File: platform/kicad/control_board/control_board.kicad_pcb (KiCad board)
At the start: 2 copper layers, 51 parts, among them J1 DHT22, J10 USB_PWR_IN, J11 UART, J12 ADC1,6, J13 24V/5V OUT, J14 PoE 1, J15 PoE 2, J16 PoE 3, J17 Barrel_Jack, J18 ADC1,7, J19 ROUTER 24V, J2 DS18B20, J3 Qwiic JST, J4 Qwiic JST, J5 Nav Light, J6 24V IN, J7 RJ45 IN - 1, J8 RJ45 IN - 2, J9 RJ45 IN - 3, K0 LCA717, K1 LCA717, K2 LCA717, K3 LCA717, M1 STEPDOWN->5V, U2 ESP32-DevKitC, U3 ACS722xLCTR-20AU

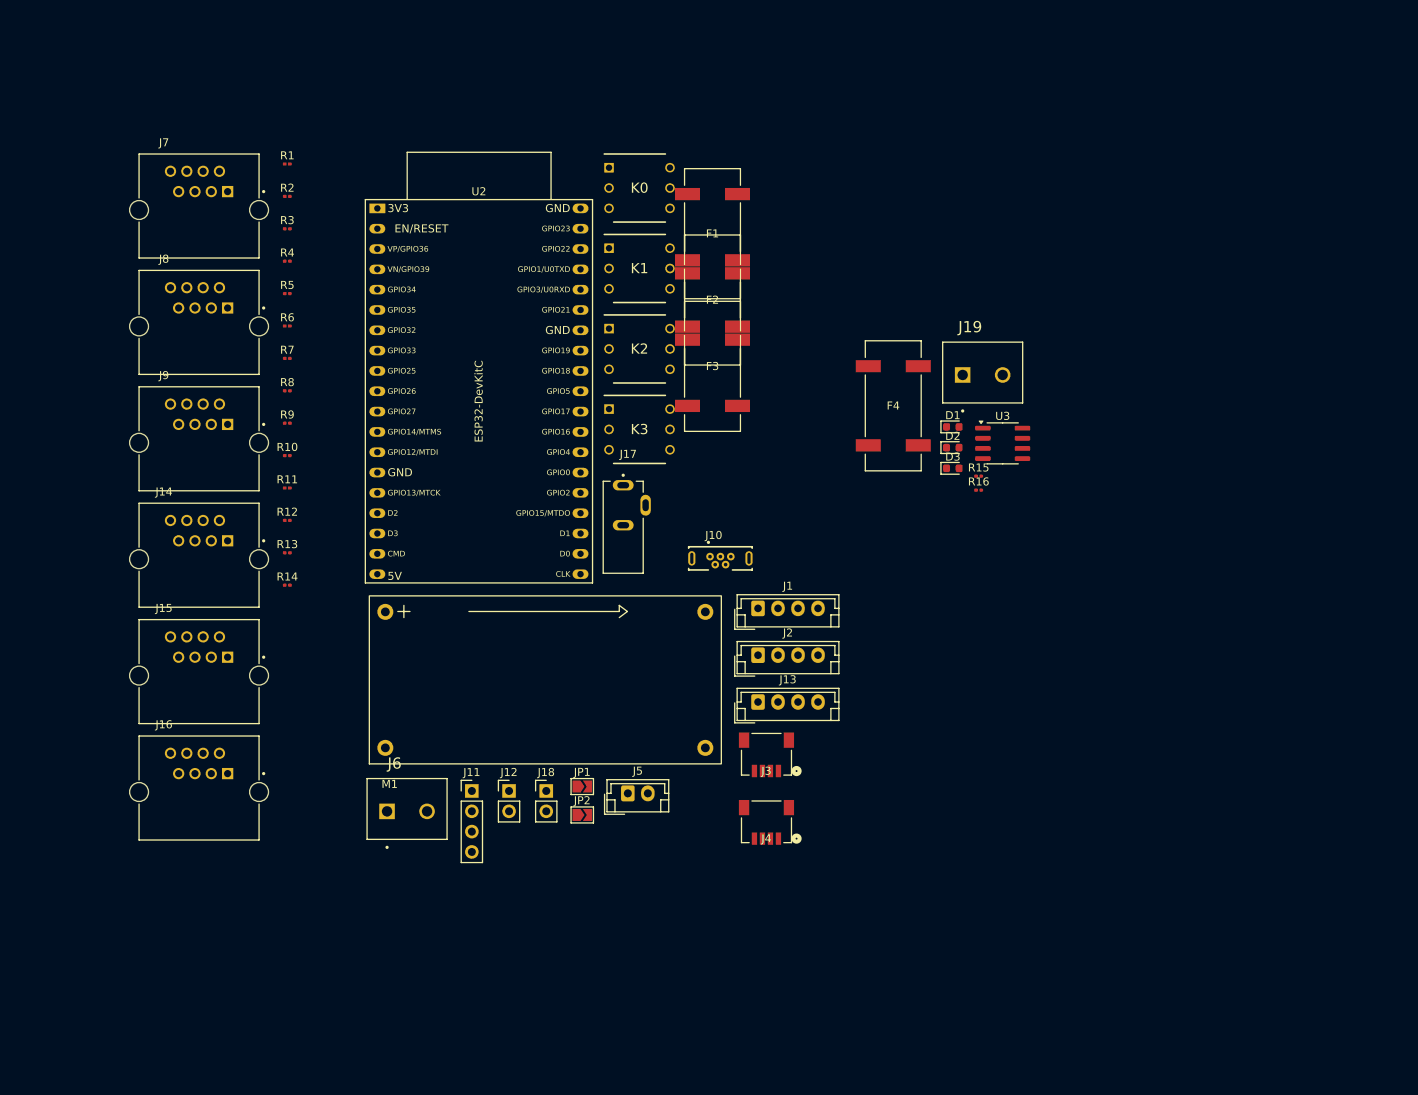
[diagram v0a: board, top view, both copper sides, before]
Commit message: Control Board: Add all 3d models and complete initial layout (#3)
This change adds a new models directory which contains the 3d models for the footprints used in PCBs.
This change also completes a draft layout for the new PCB.
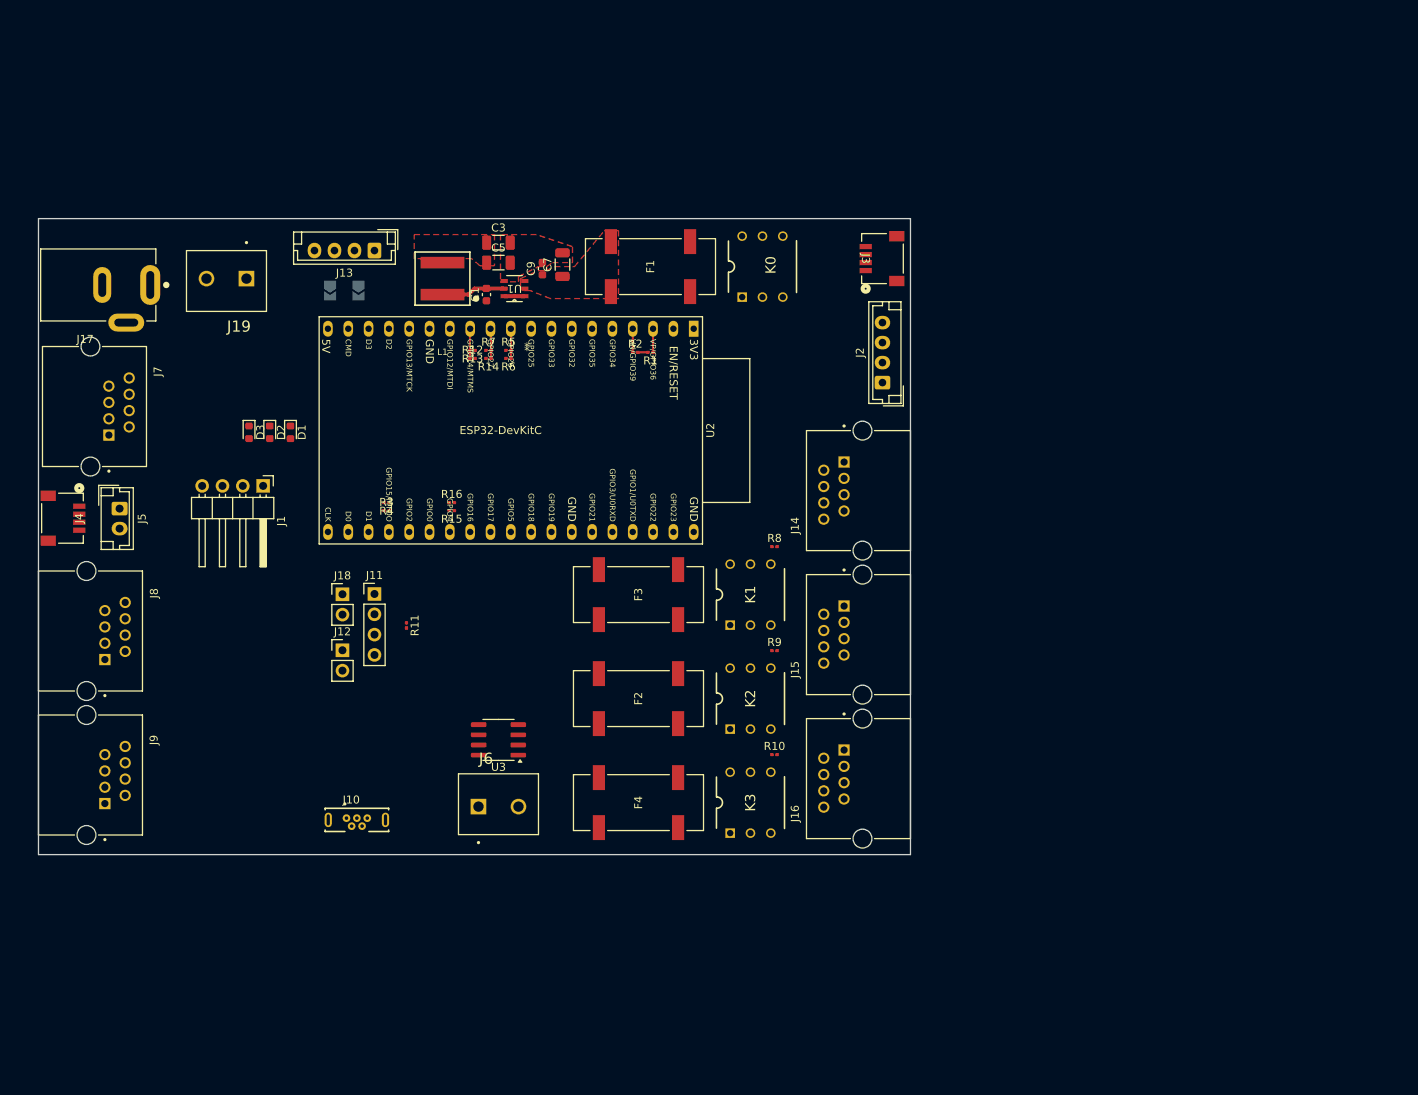
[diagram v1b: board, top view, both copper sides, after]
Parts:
- removed M1: STEPDOWN->5V, AusOcean:LM2596_Step_Down_Module
- added C1: 0.1u, Capacitor_SMD:C_0603_1608Metric, F.Cu at (143.0, 59.5)
- added C3: 22u, Capacitor_SMD:C_1206_3216Metric, F.Cu at (144.5, 53.0)
- added C5: 22u, Capacitor_SMD:C_1206_3216Metric, F.Cu at (144.5, 55.5)
- added C7: 10u, Capacitor_SMD:C_1206_3216Metric, F.Cu at (152.5, 55.8)
- added C9: 0.1u, Capacitor_SMD:C_0603_1608Metric, F.Cu at (150.0, 56.2)
- added L1: 6.8u, AusOcean:WE-XHMI_6060, F.Cu at (137.5, 57.5)
- added U1: AP63205WU-7, AusOcean:SOIC_05WU-7_DIO, F.Cu at (146.5, 58.8)
- J1: footprint Connector_JST:JST_EH_B4B-EH-A_1x04_P2.50mm_Vertical -> Connector_PinHeader_2.54mm:PinHeader_1x04_P2.54mm_Horizontal
- J17: value Barrel_Jack -> PJ-002A; footprint AusOcean:3.5x1.35mm_Barrel_Jack_Port -> AusOcean:CUI_PJ-002A
- JP1, JP2: moved to B.Cu
- moved J4 95.8 mm to (90.0, 87.5), turned to 90 degrees
- moved J19 90.3 mm to (113.0, 57.5), turned to 180 degrees
- moved D3 88.1 mm to (113.3, 76.7), turned to -90 degrees
- moved D2 85.4 mm to (115.9, 76.7), turned to -90 degrees
- moved J14 83.4 mm to (190.0, 84.0), turned to 90 degrees
- moved J15 83.1 mm to (190.0, 102.0), turned to 90 degrees
- moved J16 82.9 mm to (190.0, 120.0), turned to 90 degrees
- moved D1 82.8 mm to (118.5, 76.7), turned to -90 degrees
- moved J13 74.0 mm to (129.0, 54.0), turned to 180 degrees
- moved U3 73.1 mm to (144.5, 115.2), turned to 180 degrees
- moved J5 72.8 mm to (97.1, 86.2), turned to -90 degrees
- moved R10 71.5 mm to (179.0, 117.0)
- moved JP2 71.3 mm to (127.0, 59.0), turned to -90 degrees
- moved JP1 69.6 mm to (123.5, 59.0), turned to -90 degrees
- moved R9 67.2 mm to (179.0, 104.0)
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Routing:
- net Net-(U1-SW): track 0.00 -> 8.01 mm
- net _P2_out: track 0.00 -> 3.73 mm
- net _P3_out: track 0.00 -> 3.71 mm
- net _P1_out: track 0.00 -> 3.71 mm
- net SST: track 0.00 -> 2.95 mm
- net DHT: track 0.00 -> 2.95 mm
- net Net-(U1-BST): track 0.00 -> 2.60 mm
- net 5VIN: track 0.00 -> 1.26 mm
- added copper zone on F.Cu, net GND
- added copper zone on F.Cu, net NW_5V
- added copper zone on F.Cu, net NW_out
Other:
- board outline added: 109 x 79.5 mm

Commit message: Control PCB: Update layout (#3)
This change updates the layout of the PCB to revise the feedback from the previous iteration.
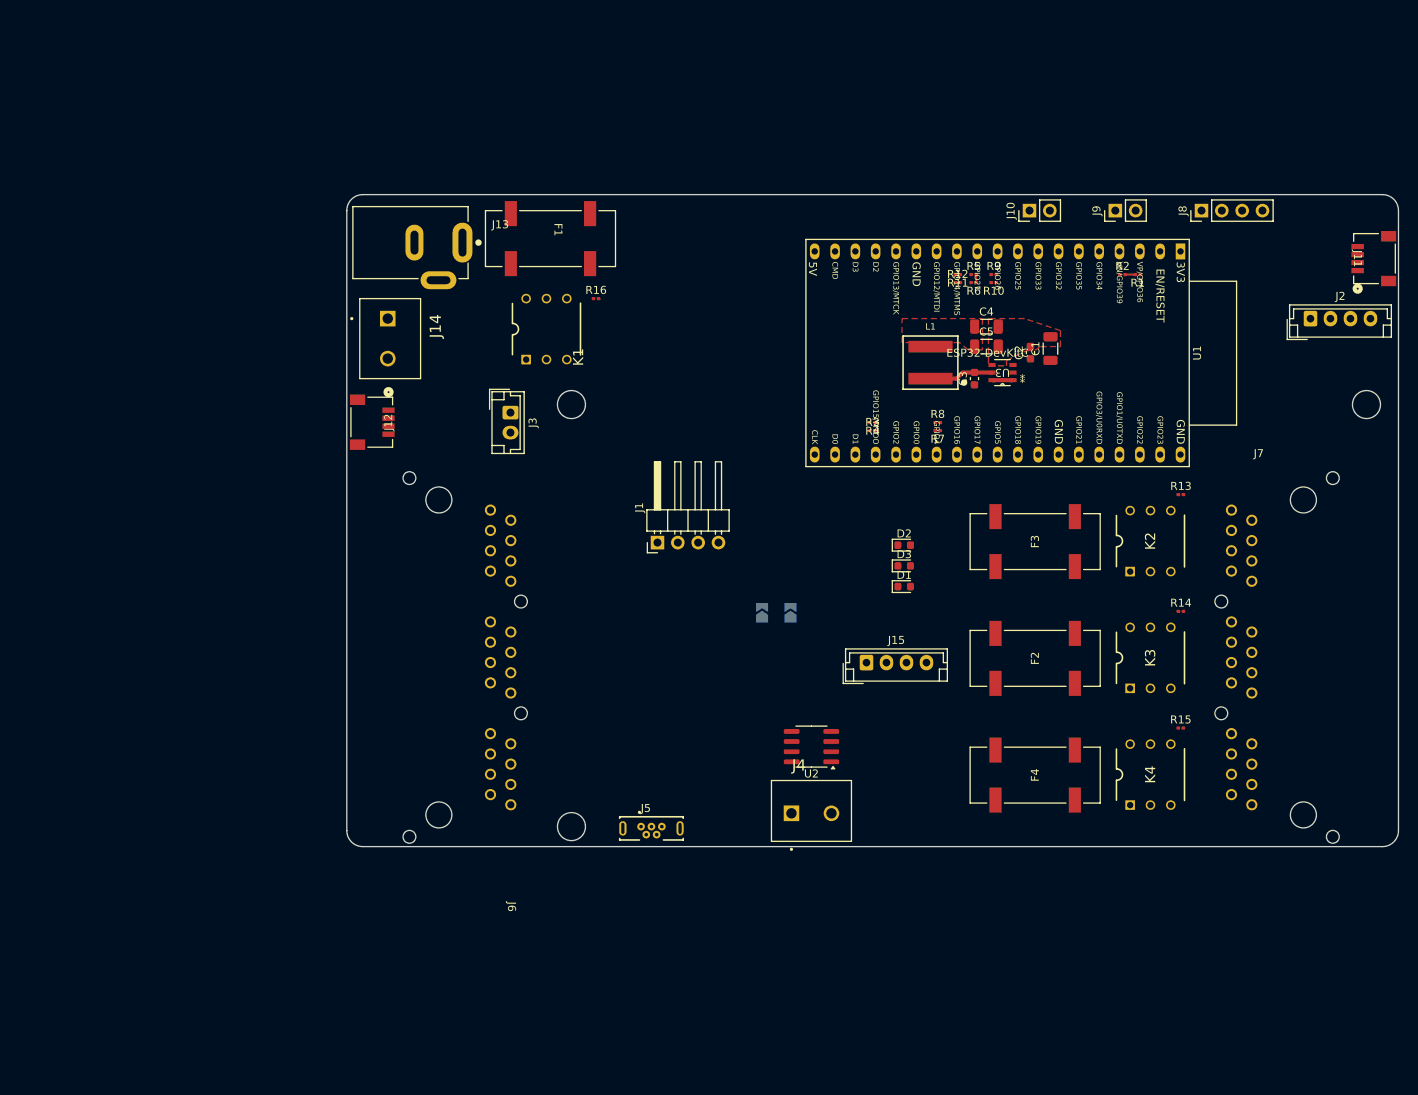
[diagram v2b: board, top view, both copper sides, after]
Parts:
- removed the J14 at (190.0, 84.0)
- removed the J15 at (190.0, 102.0)
- removed J16: PoE 3, AusOcean:RJ45_Socket
- removed the J8 at (93.0, 101.5)
- removed the J9 at (93.0, 119.5)
- added J6: ~, AusOcean:RJ45 3-port jack, F.Cu at (126.2, 82.3)
- J7: value RJ45 IN - 1 -> ~; footprint AusOcean:RJ45_Socket -> AusOcean:RJ45 3-port jack
- moved J7 171.2 mm to (256.0, 127.4), turned to 90 degrees
- moved J8 113.9 mm to (232.4, 49.0), turned to 90 degrees
- moved J9 111.1 mm to (221.6, 49.0), turned to 90 degrees
- moved J10 98.4 mm to (210.9, 49.0), turned to 90 degrees
- moved D1 84.1 mm to (195.2, 96.0), turned to 0 degrees
- moved D3 81.0 mm to (195.2, 93.4), turned to 0 degrees
- moved J15 80.2 mm to (190.5, 105.5), turned to 0 degrees
- moved D2 78.0 mm to (195.2, 90.8), turned to 0 degrees
- moved JP1 70.2 mm to (181.0, 99.3), turned to 90 degrees
- moved JP2 64.6 mm to (177.4, 99.3), turned to 90 degrees
- moved C1 61.9 mm to (213.5, 66.2)
- moved C2 61.9 mm to (211.0, 66.8)
- moved C3 61.9 mm to (204.0, 70.0)
- moved C4 61.9 mm to (205.5, 63.5)
- moved C5 61.9 mm to (205.5, 66.0)
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- renumbered C7 to C1, C9 to C2, C1 to C3, C3 to C4, D3 to D1, D1 to D2, D2 to D3, J18 to J10, J3 to J11, J4 to J12, J17 to J13, J19 to J14, J13 to J15, J5 to J3, J6 to J4, J10 to J5, J11 to J8, J12 to J9, K0 to K1, K1 to K2, K2 to K3, K3 to K4, R6 to R10, R13 to R11, R8 to R13, R9 to R14, R10 to R15, R11 to R16, R7 to R5, R14 to R6, R15 to R7, R16 to R8, R5 to R9, U2 to U1, U3 to U2, U1 to U3
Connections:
- J7 pad 1: D1_Rx+ -> D3_Rx+
- J7 pad 2: D1_Rx- -> D3_Rx-
- J7 pad 3: D1_Tx+ -> D3_Tx+
- J7 pad 4: unconnected-(J7-Pad4) -> P3_out
- J7 pad 5: unconnected-(J7-Pad5) -> P3_out
- J7 pad 6: D1_Tx- -> D3_Tx-
- J7 pad 7: unconnected-(J7-Pad7) -> GND
- J7 pad 8: unconnected-(J7-Pad8) -> GND
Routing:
- net _P1_out: track 3.71 -> 0.04 mm
- net _P3_out: track 3.71 -> 0.05 mm
- net SST: track 2.95 -> 0.00 mm
- net DHT: track 2.95 -> 0.00 mm
- net _P2_out: track 3.73 -> 1.09 mm
- removed copper zone on F.Cu, net NW_out
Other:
- board size 109 x 79.5 mm -> 131.5 x 81.5 mm

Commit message: Update Control Board layout
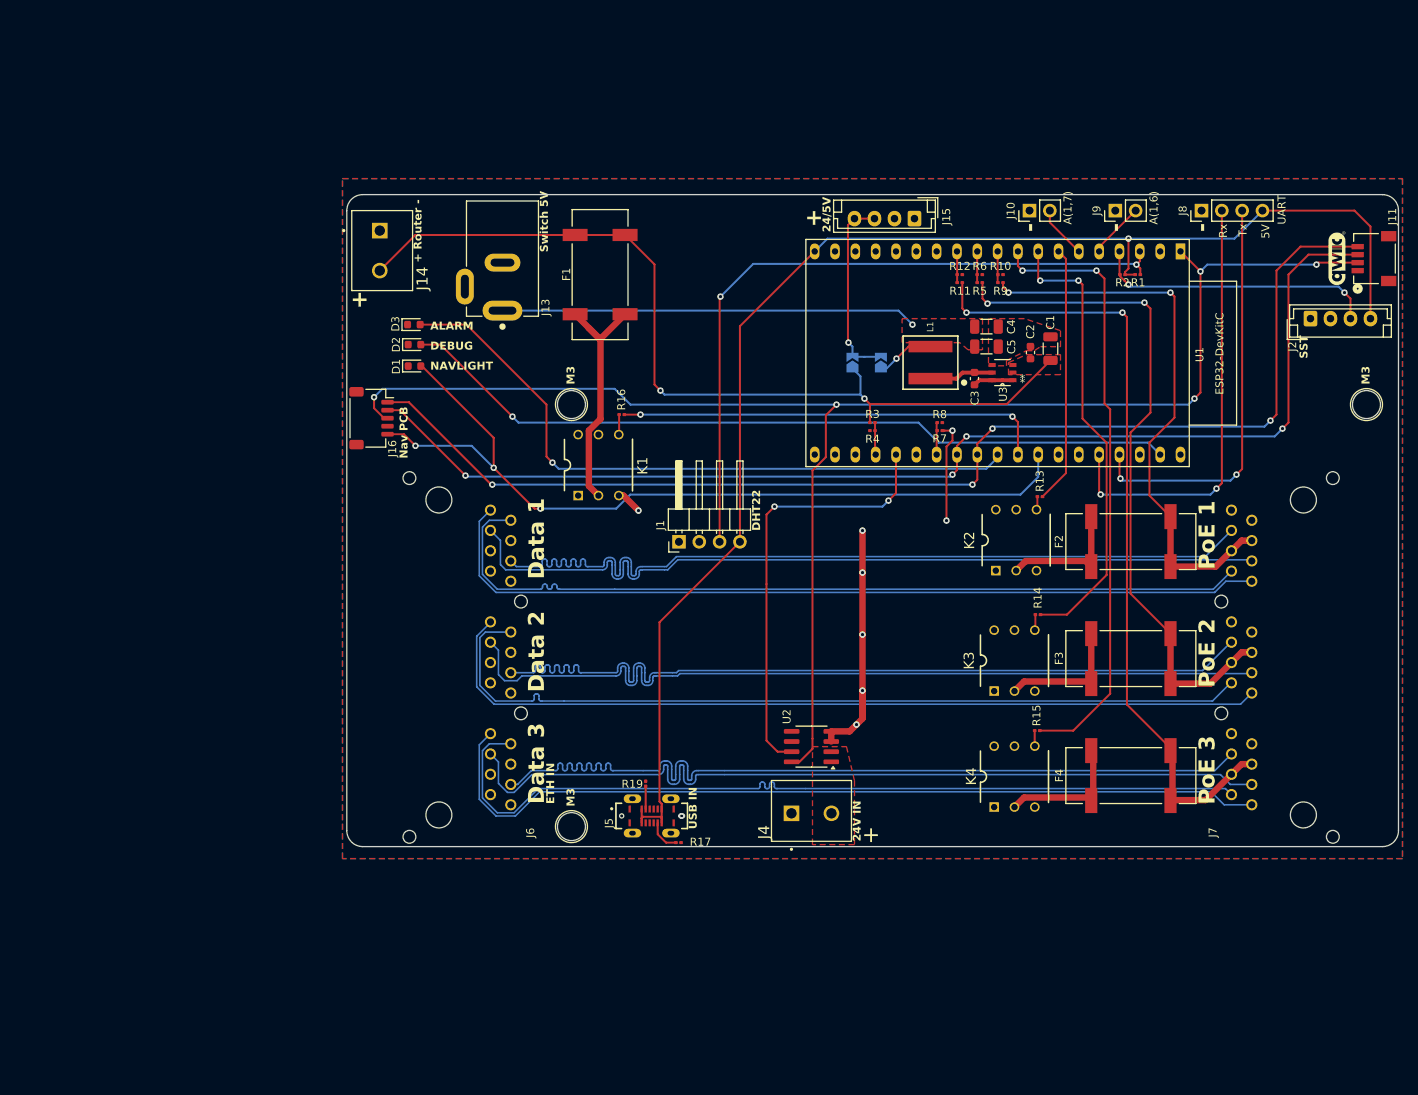
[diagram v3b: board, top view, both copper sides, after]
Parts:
- removed J12: Qwiic JST, AusOcean:CONN_SM04B-SRSS-TB_JST
- removed J3: Nav Light, Connector_JST:JST_EH_B2B-EH-A_1x02_P2.50mm_Vertical
- added G***: LOGO, LOGO, F.Cu at (249.2, 55.0)
- added J16: Conn_01x05_Pin, Connector_JST:JST_SH_SM05B-SRSS-TB_1x05-1MP_P1.00mm_Horizontal, F.Cu at (128.6, 75.0)
- added R17: 5.1K, Resistor_SMD:R_0201_0603Metric, F.Cu at (167.0, 128.0)
- added R19: 5.1K, Resistor_SMD:R_0201_0603Metric, F.Cu at (162.9, 120.6)
- J5: value USB_PWR_IN -> USB4120-03-C_REVA; footprint AusOcean:USB_Micro_B_CONN -> AusOcean:GCT_USB4120-03-C_REVA
- moved D3 68.3 mm to (133.9, 63.2)
- moved D1 67.1 mm to (134.0, 68.4)
- moved D2 66.1 mm to (134.0, 65.8)
- moved J15 55.8 mm to (196.5, 50.0), turned to 180 degrees
- moved JP1 33.3 mm to (192.3, 68.0)
- moved JP2 33.3 mm to (188.8, 68.0)
- moved F3 18.9 mm to (223.5, 105.0), turned to -90 degrees
- moved F2 18.9 mm to (223.5, 90.4), turned to -90 degrees
- moved K1 18.2 mm to (157.0, 80.8)
- moved R15 17.9 mm to (211.8, 114.0)
- moved R14 17.9 mm to (211.9, 99.5)
- moved R13 17.6 mm to (212.2, 84.8)
- moved K3 17.0 mm to (209.0, 105.2)
- moved K4 17.0 mm to (209.0, 119.8)
- moved K2 16.8 mm to (209.2, 90.2)
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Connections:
- F2 pad 3: 24VIN -> Net-(K2--_LOAD)
- F2 pad 4: 24VIN -> Net-(K2--_LOAD)
- F3 pad 3: 24VIN -> Net-(K3--_LOAD)
- F3 pad 4: 24VIN -> Net-(K3--_LOAD)
- F4 pad 3: 24VIN -> Net-(K4--_LOAD)
- F4 pad 4: 24VIN -> Net-(K4--_LOAD)
- J11 pad 4: SCl -> SCL
- J5 pad S1: (no net) -> GND
- J5 pad S2: (no net) -> GND
- K2 pad 2: 24VIN -> Net-(K2--_LOAD)
- K3 pad 2: 24VIN -> Net-(K3--_LOAD)
- K4 pad 2: 24VIN -> Net-(K4--_LOAD)
- U1 pad 33: SDA -> unconnected-(U1-GPIO21-Pad33)
- U1 pad 36: SCL -> unconnected-(U1-GPIO22-Pad36)
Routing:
- net +3V3: track 0.00 -> 195.2 mm, vias 0 -> 5
- net 5VIN: track 1.26 -> 174.0 mm, vias 0 -> 1
- net SCL: track 0.00 -> 151.0 mm, vias 0 -> 4
- net SDA: track 0.00 -> 148.8 mm, vias 0 -> 4
- net NW_out: track 0.00 -> 111.5 mm, vias 0 -> 2
- net D3_Rx+: track 0.00 -> 108.1 mm
- net D3_Rx-: track 0.00 -> 108.1 mm
- net D3_Tx+: track 0.00 -> 108.0 mm
- net D3_Tx-: track 0.00 -> 107.7 mm
- net D2_Rx+: track 0.00 -> 107.2 mm
- net D2_Rx-: track 0.00 -> 107.2 mm
- net D2_Tx+: track 0.00 -> 107.0 mm
- net D2_Tx-: track 0.00 -> 106.8 mm
- net D1_Rx+: track 0.00 -> 106.8 mm
- net D1_Tx+: track 0.00 -> 106.7 mm
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- added copper zone on B.Cu, net 24VIN
- added copper zone on F.Cu, net 24VIN_IP
- added copper zone on F.Cu, net NW_out
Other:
- board text added: "+"
- board text added: "+ Router -"
- board text added: "-"
- board text added: "24/5V"
- board text added: "24V IN"
- board text added: "5V"
- board text added: "A(1,6)"
- board text added: "A(1,7)"
- board text added: "ALARM"
- board text added: "DEBUG"
- board text added: "DHT22"
- board text added: "Data 1"
- board text added: "Data 2"
- board text added: "Data 3"
- board text added: "ETH IN"
- board text added: "M3"
- board text added: "NAVLIGHT"
- board text added: "Nav PCB"
- board text added: "PoE 1"
- board text added: "PoE 2"
- board text added: "PoE 3"
- board text added: "Rx"
- board text added: "SST"
- board text added: "Switch 5V"
- board text added: "Tx"
- board text added: "UART"
- board text added: "USB IN"
